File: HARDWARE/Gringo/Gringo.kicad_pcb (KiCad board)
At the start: 2 copper layers, 201 x 48 mm, 62 parts, among them J1 Conn_01x06, J10 Conn_01x06, J11 Conn_01x06, J12 Conn_01x06, J13 Conn_01x05_Pin, J2 Conn_01x06, J3 Conn_01x06, J4 Alim, J5 Conn_01x06, J6 Conn_01x06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

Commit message: Update holes
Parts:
- removed the ? at (214.2, 110.2)
- removed the ? at (153.2, 98.2)
- removed the ? at (214.2, 104.2)
- removed the ? at (153.2, 104.2)
- removed the ? at (99.7, 74.2)
- removed the ? at (153.2, 92.2)
- removed the ? at (99.7, 110.2)
- removed the ? at (153.2, 80.2)
- removed the ? at (99.7, 92.2)
- removed the ? at (214.2, 92.2)
- removed the ? at (214.2, 98.2)
- removed the ? at (99.7, 80.2)
- removed the ? at (99.7, 98.2)
- removed the ? at (153.2, 74.2)
- removed the ? at (99.7, 104.2)
- removed the ? at (153.2, 110.2)
- removed the ? at (153.2, 86.2)
- removed the ? at (99.7, 86.2)
- removed the REF** at (153.2, 68.2)
- removed the REF** at (99.7, 68.2)
- added ?: , , F.Cu at (153.0, 92.0)
- added ?: , , F.Cu at (214.2, 109.9)
- added ?: , , F.Cu at (99.7, 110.1)
- added ?: , , F.Cu at (153.0, 80.4)
- added ?: , , F.Cu at (214.2, 103.9)
- added ?: , , F.Cu at (153.0, 74.4)
- added ?: , , F.Cu at (99.7, 104.1)
- added ?: , , F.Cu at (153.0, 104.0)
- added ?: , , F.Cu at (153.0, 86.4)
- added ?: , , F.Cu at (214.2, 97.9)
- added ?: , , F.Cu at (99.7, 74.5)
- added ?: , , F.Cu at (153.0, 98.0)
- added ?: , , F.Cu at (153.0, 110.0)
- added ?: , , F.Cu at (99.7, 86.5)
- added ?: , , F.Cu at (99.7, 98.1)
- added ?: , , F.Cu at (99.7, 92.1)
- added ?: , , F.Cu at (214.2, 91.9)
- added ?: , , F.Cu at (99.7, 80.5)
- added REF**: MountingHole_4mm, MountingHole:MountingHole_4mm, F.Cu at (153.0, 68.4)
- added REF**: MountingHole_4mm, MountingHole:MountingHole_4mm, F.Cu at (99.7, 68.5)

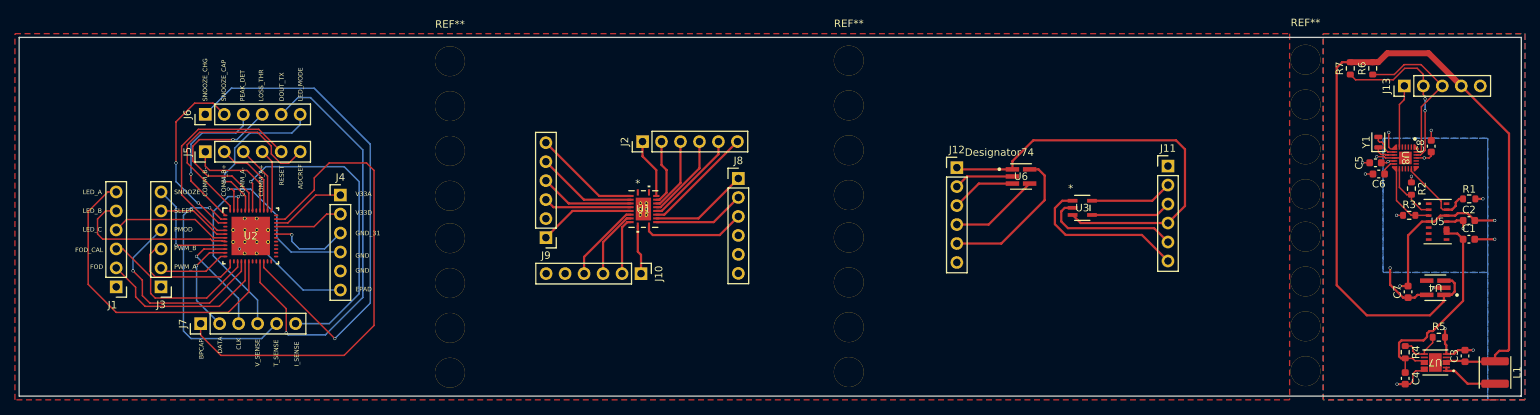
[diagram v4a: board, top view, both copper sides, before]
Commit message: Update the quartz model
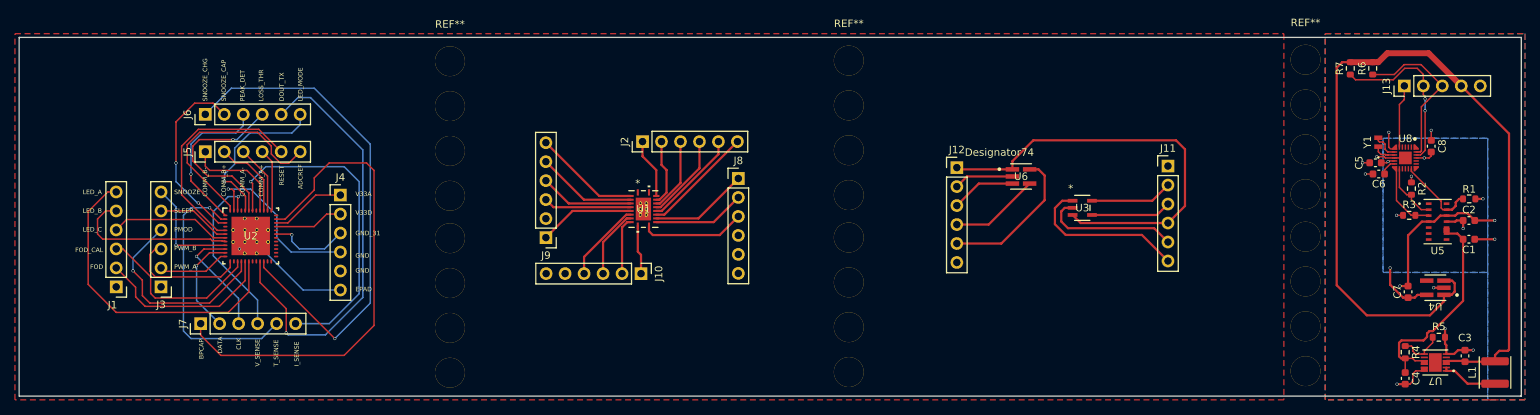
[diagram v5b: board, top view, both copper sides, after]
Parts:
- Y1: footprint Crystal:Crystal_SMD_2012-2Pin_2.0x1.2mm -> ECS-327-12-5-12-TR:XTAL_ECX-12_2X1P2_ECS
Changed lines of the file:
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@@
 		(embedded_fonts no)
 	)
-	(footprint "Crystal:Crystal_SMD_2012-2Pin_2.0x1.2mm"
+	(footprint "ECS-327-12-5-12-TR:XTAL_ECX-12_2X1P2_ECS"
 		(layer "F.Cu")
 		(at 223.89 79.29 90)
-		(descr "2012/2, Crystal, 2.0x1.2mm package, SMD, generated with kicad-footprint-generator make_crystal.py, http://txccrystal.com/images/pdf/9ht11.pdf")
+		(tags "ECS-.327-12.5-12-TR ")
 		(property "Reference" "Y1"
-			(at 0.01 -1.62 90)
+			(at 0 -1.45 90)
+			(unlocked yes)
 			(layer "F.SilkS")
 			(effects
@@
 		)
 		(property "Value" "32k768"
-			(at 0 1.8 90)
+			(at 0 0 90)
+			(unlocked yes)
 			(layer "F.Fab")
 			(effects
@@
 		(sheetfile "bpm-module.kicad_sch")
 		(attr smd)
-		(fp_line
-			(start 1.26 -0.86)
-			(end -1.26 -0.86)
+		(fp_circle
+			(center -2.0574 0)
+			(end -1.9812 0)
 			(stroke
-				(width 0.12)
+				(width 0.1524)
 				(type solid)
 			)
+			(fill no)
 			(layer "F.SilkS")
 		)
 		(fp_line
-			(start -1.26 -0.86)
-			(end -1.26 0.86)
+			(start 1.2573 -0.8509)
+			(end 1.2573 -0.8001)
 			(stroke
-				(width 0.12)
+				(width 0.1524)
 				(type solid)
 			)
-			(layer "F.SilkS")
+			(layer "F.CrtYd")
 		)
 		(fp_line
-			(start -1.26 0.86)
-			(end 1.26 0.86)
+			(start -1.2573 -0.8509)
+			(end 1.2573 -0.8509)
 			(stroke
-				(width 0.12)
+				(width 0.1524)
 				(type solid)
 			)
-			(layer "F.SilkS")
+			(layer "F.CrtYd")
 		)
-		(fp_circle
-			(center 0 0)
-			(end 0.2 0)
+		(fp_line
+			(start 1.2573 -0.8001)
+			(end 1.2573 -0.8001)
 			(stroke
-				(width 0.1)
+				(width 0.1524)
 				(type solid)
 			)
-			(fill yes)
-			(layer "F.Adhes")
+			(layer "F.CrtYd")
 		)
-		(fp_rect
-			(start -1.5 -1.1)
-			(end 1.5 1.1)
+		(fp_line
+			(start 1.2573 -0.8001)
+			(end 1.2573 0.8001)
 			(stroke
-				(width 0.05)
+				(width 0.1524)
 				(type solid)
 			)
-			(fill no)
 			(layer "F.CrtYd")
 		)
-		(fp_poly
-			(pts
-				(xy -1 -0.6) (xy -1 0.3) (xy -0.7 0.6) (xy 1 0.6) (xy 1 -0.6)
+		(fp_line
+			(start -1.2573 -0.8001)
+			(end -1.2573 -0.8509)
+			(stroke
+				(width 0.1524)
+				(type solid)
 			)
+			(layer "F.CrtYd")
+		)
+		(fp_line
+			(start -1.2573 -0.8001)
+			(end -1.2573 -0.8001)
 			(stroke
-				(width 0.1)
+				(width 0.1524)
+				(type solid)
+			)
+			(layer "F.CrtYd")
+		)
+		(fp_line
+			(start 1.2573 0.8001)
+			(end 1.2573 0.8001)
+			(stroke
+				(width 0.1524)
+				(type solid)
+			)
+			(layer "F.CrtYd")
+		)
+		(fp_line
+			(start 1.2573 0.8001)
+			(end 1.2573 0.8509)
+			(stroke
+				(width 0.1524)
+				(type solid)
+			)
+			(layer "F.CrtYd")
+		)
+		(fp_line
+			(start -1.2573 0.8001)
+			(end -1.2573 -0.8001)
+			(stroke
+				(width 0.1524)
+				(type solid)
+			)
+			(layer "F.CrtYd")
+		)
+		(fp_line
+			(start -1.2573 0.8001)
+			(end -1.2573 0.8001)
+			(stroke
+				(width 0.1524)
+				(type solid)
+			)
+			(layer "F.CrtYd")
+		)
+		(fp_line
+			(start 1.2573 0.8509)
+			(end -1.2573 0.8509)
+			(stroke
+				(width 0.1524)
+				(type solid)
+			)
+			(layer "F.CrtYd")
+		)
+		(fp_line
+			(start -1.2573 0.8509)
+			(end -1.2573 0.8001)
+			(stroke
+				(width 0.1524)
+				(type solid)
+			)
+			(layer "F.CrtYd")
+		)
+		(fp_line
+			(start 1.0033 -0.5969)
+			(end -1.0033 -0.5969)
+			(stroke
+				(width 0.0254)
+				(type solid)
+			)
+			(layer "F.Fab")
+		)
+		(fp_line
+			(start -1.0033 -0.5969)
+			(end -1.0033 0.5969)
+			(stroke
+				(width 0.0254)
+				(type solid)
+			)
+			(layer "F.Fab")
+		)
+		(fp_line
+			(start 1.0033 0.5969)
+			(end 1.0033 -0.5969)
+			(stroke
+				(width 0.0254)
+				(type solid)
+			)
+			(layer "F.Fab")
+		)
+		(fp_line
+			(start -1.0033 0.5969)
+			(end 1.0033 0.5969)
+			(stroke
+				(width 0.0254)
+				(type solid)
+			)
+			(layer "F.Fab")
+		)
+		(fp_circle
+			(center 0 0)
+			(end 0.0762 0)
+			(stroke
+				(width 0.0254)
 				(type solid)
 			)
@@
 		(fp_text user "${REFERENCE}"
 			(at 0 0 90)
+			(unlocked yes)
 			(layer "F.Fab")
 			(effects
 				(font
-					(size 0.5 0.5)
-					(thickness 0.08)
+					(size 1 1)
+					(thickness 0.15)
 				)
 			)
 		)
-		(pad "1" smd roundrect
-			(at -0.7 0 90)
-			(size 0.6 1.1)
+		(pad "1" smd rect
+			(at -0.5969 0 90)
+			(size 0.6096 1.0922)
 			(layers "F.Cu" "F.Mask" "F.Paste")
-			(roundrect_rratio 0.25)
 			(net 94 "Net-(U8A-32KIN)")
 			(pinfunction "1")
 			(pintype "passive")
 		)
-		(pad "2" smd roundrect
-			(at 0.7 0 90)
-			(size 0.6 1.1)
+		(pad "2" smd rect
+			(at 0.5969 0 90)
+			(size 0.6096 1.0922)
 			(layers "F.Cu" "F.Mask" "F.Paste")
-			(roundrect_rratio 0.25)
 			(net 98 "Net-(U8A-32KOUT)")
 			(pinfunction "2")
@@
 		)
 		(embedded_fonts no)
-		(model "${KICAD9_3DMODEL_DIR}/Crystal.3dshapes/Crystal_SMD_2012-2Pin_2.0x1.2mm.step"
-			(offset
-				(xyz 0 0 0)
-			)
-			(scale
-				(xyz 1 1 1)
-			)
-			(rotate
-				(xyz 0 0 0)
-			)
-		)
 	)
 	(footprint "Resistor_SMD:R_0603_1608Metric"
@@
 		(tags "capacitor")
 		(property "Reference" "C8"
-			(at 0 -1.43 90)
+			(at 0 1.4691 90)
 			(layer "F.SilkS")
 			(effects
@@
 		(tags "PTPS7A2018PDBVR ")
 		(property "Reference" "U4"
-			(at 0 0 180)
+			(at 0 -2.5 180)
 			(unlocked yes)
 			(layer "F.SilkS")
@@
 		(tags "capacitor")
 		(property "Reference" "C1"
-			(at 0 -1.43 0)
+			(at 0 1.4 0)
 			(layer "F.SilkS")
 			(effects
@@
 		(tags "wirewound power shielded")
 		(property "Reference" "L1"
-			(at 0 -2.95 90)
+			(at 0 3.05 90)
 			(layer "F.SilkS")
 			(effects
@@
 		(tags "PAM2401YPADJ ")
 		(property "Reference" "U7"
-			(at 0 0 180)
+			(at 0 -2.47 180)
 			(unlocked yes)
 			(layer "F.SilkS")
@@
 		(fp_text user "*"
 			(at -0.75 -1.800001 0)
+			(unlocked yes)
 			(layer "F.Fab")
 			(effects
@@
 		(fp_text user "*"
 			(at -0.75 -1.800001 0)
-			(unlocked yes)
 			(layer "F.Fab")
 			(effects
@@
 		(tags "capacitor")
 		(property "Reference" "C3"
-			(at 0 -1.43 90)
+			(at 2.425002 -0.01 180)
 			(layer "F.SilkS")
 			(effects
@@
 			)
 		)
-		(fp_text user "*"
-			(at -0.6477 -1.6358 0)
+		(fp_text user "${REFERENCE}"
+			(at 0 0 0)
+			(unlocked yes)
 			(layer "F.Fab")
 			(effects
@@
 			)
 		)
-		(fp_text user "${REFERENCE}"
-			(at 0 0 0)
+		(fp_text user "*"
+			(at -0.6477 -1.6358 0)
 			(unlocked yes)
 			(layer "F.Fab")
@@
 		(fp_text user "*"
 			(at -0.6477 -1.6358 0)
-			(unlocked yes)
 			(layer "F.Fab")
 			(effects
@@
 		(tags "MAX32664GTGA+T ")
 		(property "Reference" "U8"
-			(at 0 0 270)
+			(at -2.59 0 0)
 			(unlocked yes)
 			(layer "F.SilkS")
@@
 		(tags "MAX30101EFD+ ")
 		(property "Reference" "U5"
-			(at 0 0 0)
+			(at 0 3.899999 0)
 			(unlocked yes)
 			(layer "F.SilkS")
@@
 	)
 	(segment
-		(start 223.89 79.11)
-		(end 223.89 78.59)
+		(start 224.51 79.27)
+		(end 224.05 79.27)
 		(width 0.2)
 		(layer "F.Cu")
@@
 	)
 	(segment
-		(start 224.641 79.561)
-		(end 224.35 79.27)
+		(start 223.89 79.11)
+		(end 223.89 78.59)
 		(width 0.2)
 		(layer "F.Cu")
@@
 	)
 	(segment
-		(start 224.35 79.27)
-		(end 224.05 79.27)
+		(start 224.79 80.24)
+		(end 224.79 79.55)
 		(width 0.2)
 		(layer "F.Cu")
@@
 	)
 	(segment
-		(start 224.641 80.091)
-		(end 224.641 79.561)
+		(start 224.05 79.27)
+		(end 223.89 79.11)
 		(width 0.2)
 		(layer "F.Cu")
@@
 	)
 	(segment
-		(start 224.05 79.27)
-		(end 223.89 79.11)
+		(start 224.79 79.55)
+		(end 224.51 79.27)
 		(width 0.2)
 		(layer "F.Cu")
@@
 	(segment
 		(start 225.149999 80.599999)
-		(end 224.641 80.091)
+		(end 224.79 80.24)
 		(width 0.2)
 		(layer "F.Cu")
@@
 		(polygon
 			(pts
-				(xy 212.02 64.77) (xy 212.02 113.77) (xy 41.45 113.77) (xy 41.45 64.77)
+				(xy 211.25 64.77) (xy 211.25 113.77) (xy 41.45 113.77) (xy 41.45 64.77)
 			)
 		)
@@
 		(polygon
 			(pts
-				(xy 216.52 64.77) (xy 243.52 64.77) (xy 243.52 113.77) (xy 240 113.77) (xy 239.77 113.77) (xy 239.47 113.77)
-				(xy 239.11 113.77) (xy 238.65 113.77) (xy 238.52 113.77) (xy 216.52 113.77)
+				(xy 216.79 64.77) (xy 243.52 64.77) (xy 243.52 113.77) (xy 240 113.77) (xy 239.77 113.77) (xy 239.47 113.77)
+				(xy 239.11 113.77) (xy 238.65 113.77) (xy 238.52 113.77) (xy 216.79 113.77)
 			)
 		)
@@
 		(polygon
 			(pts
-				(xy 216.52 64.77) (xy 243.52 64.77) (xy 243.52 113.77) (xy 238.52 113.77) (xy 238.52 78.77) (xy 224.53 78.77)
-				(xy 224.53 96.72) (xy 238.52 96.72) (xy 238.52 113.77) (xy 216.52 113.77)
+				(xy 216.79 64.77) (xy 243.52 64.77) (xy 243.52 113.77) (xy 238.52 113.77) (xy 238.52 78.77) (xy 224.53 78.77)
+				(xy 224.53 96.72) (xy 238.52 96.72) (xy 238.52 113.77) (xy 216.79 113.77)
 			)
 		)
